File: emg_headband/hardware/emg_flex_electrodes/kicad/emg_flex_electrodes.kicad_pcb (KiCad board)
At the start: 2 copper layers, 303 x 43 mm, 8 parts, among them J1 TO MAIN BOARD J6

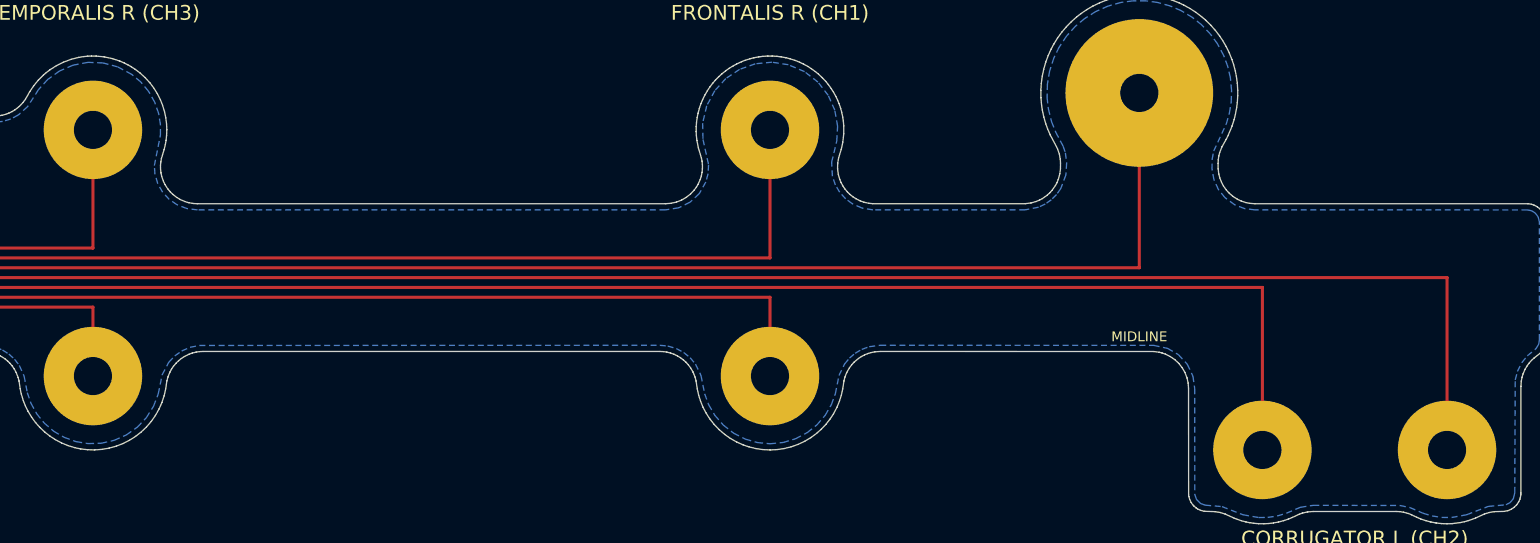
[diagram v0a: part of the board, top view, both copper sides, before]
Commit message: Flex: 2.5 mm rivet holes and JLC fab outputs
Electrode holes are 2.7 mm for a DIN 660 2.5 mm copper rivet. Re-checked
J6 against main board c72bb90 (ESP32-S3 layout): same pins, still on the
right edge, so only the tail-length note changes. Adds gerbers, drill
and a PI stiffener layer for the FPC tab, plus JLC order settings in the
README. Electrode stiffener rings are dropped for rev 1.

Co-Authored-By: Claude Opus 5.5 (1M context) <noreply@anthropic.com>
Claude-Session: https://claude.ai/code/session_014gX5rSabikoFKBd7bBuHGf
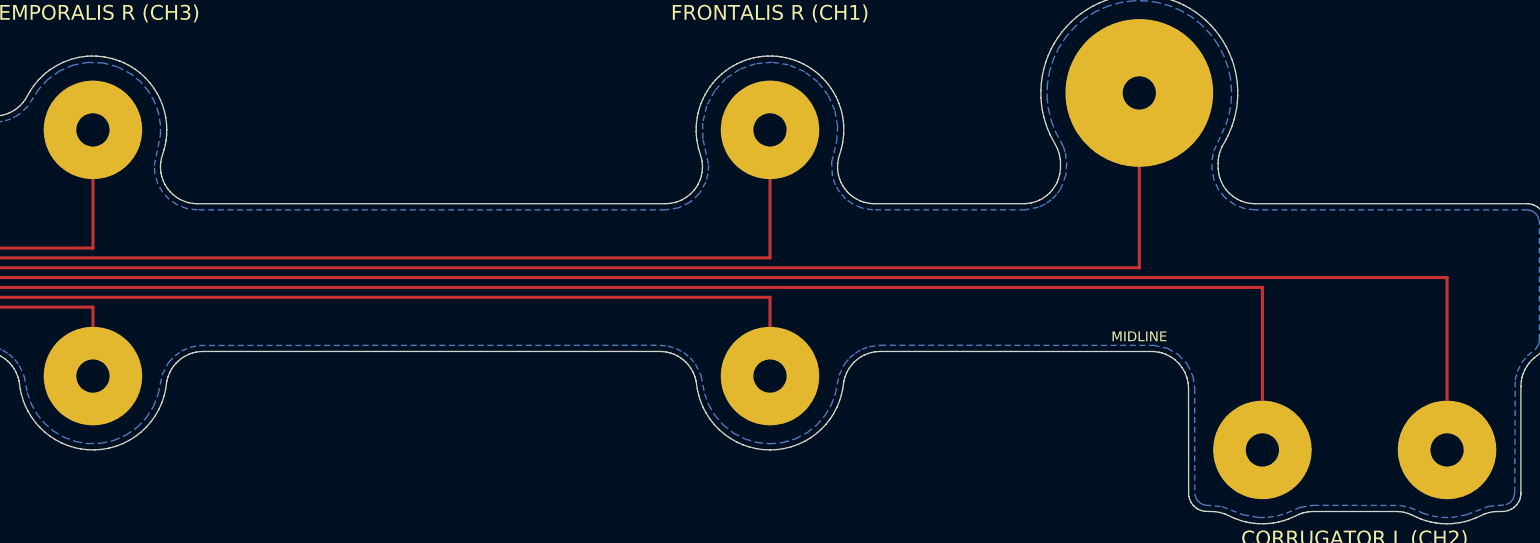
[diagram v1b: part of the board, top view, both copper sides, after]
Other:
- board text added: "STIFFENER: PI 0.2 B-SIDE"
- board text removed: "PI 0.2 B-SIDE"

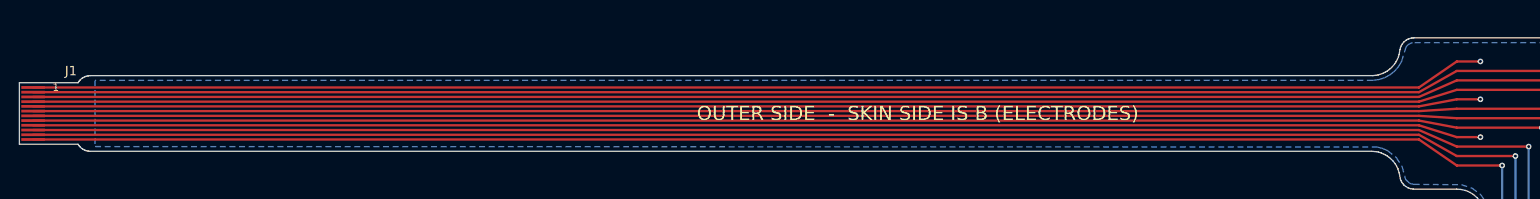
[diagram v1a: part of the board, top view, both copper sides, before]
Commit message: Flex: tie the shield to REF, leave AGND pins open
Each signal trace has ~35-55 pF to the hatched shield. On AGND that adds
to the main board's 100 pF input caps and costs dry-electrode CMRR; at
REF (RLD-driven body potential) it carries no common mode. AGND guard
lanes are removed so P and N see the same neighbours. Copper width and
thickness checked: <4 ohm per trace, noise negligible. Gerbers updated.

Co-Authored-By: Claude Opus 5.5 (1M context) <noreply@anthropic.com>
Claude-Session: https://claude.ai/code/session_014gX5rSabikoFKBd7bBuHGf
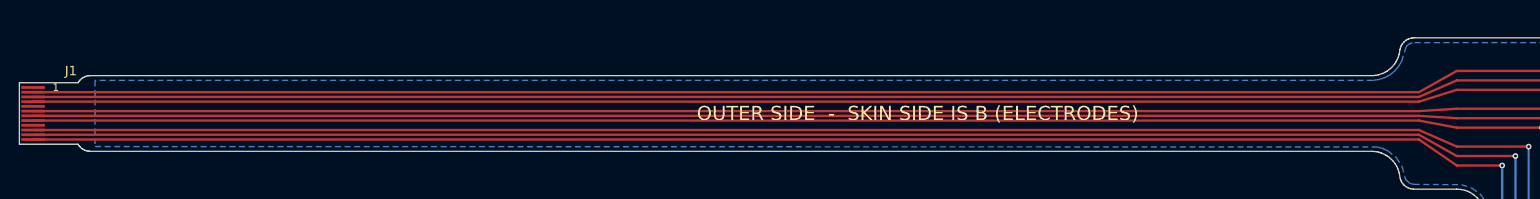
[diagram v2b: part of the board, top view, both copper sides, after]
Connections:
- J1 pad 1: AGND -> (no net)
- J1 pad 5: AGND -> (no net)
- J1 pad 9: AGND -> (no net)
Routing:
- net AGND: track 460.3 -> 0.00 mm, vias 3 -> 0
- added copper zone on B.Cu, net REF
- removed copper zone on B.Cu, net AGND
